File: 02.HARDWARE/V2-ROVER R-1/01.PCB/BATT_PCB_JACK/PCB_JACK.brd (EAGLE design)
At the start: 19.3 x 10.1 mm, 2 parts

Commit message: Connector Jack
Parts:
- removed PAD1, PAD2: WIREPADSMD2,54-5,08, wirepad:SMD2,54-5,08
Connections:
- removed net GND: PAD1.1
- removed net VCC: PAD2.1
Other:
- board size 19.3 x 10.1 mm -> 18.3 x 9.1 mm
- board text added: "+"
- board text added: "-"
- board text added: "2"

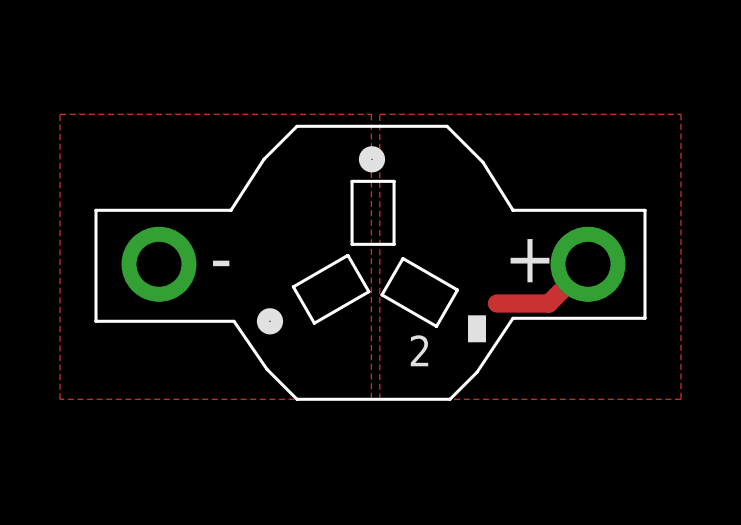
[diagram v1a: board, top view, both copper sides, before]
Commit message: Modificacion Conector Jack #37
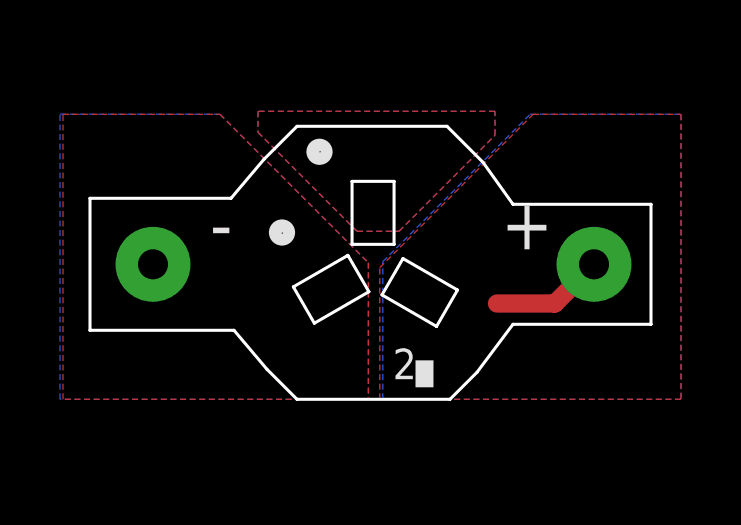
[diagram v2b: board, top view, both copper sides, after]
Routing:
- added copper zone on layer 16, net GND
- added copper zone on layer 1, net NOCONNET
- added copper zone on layer 16, net NOCONNET
- added copper zone on layer 16, net VCC
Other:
- board size 18.3 x 9.1 mm -> 18.7 x 9.1 mm

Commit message: Close #37
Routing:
- net VCC: vias 1 -> 5
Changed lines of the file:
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@@
 <grid distance="0.1" unitdist="mm" unit="mm" style="lines" multiple="1" display="yes" altdistance="5" altunitdist="mil" altunit="mil"/>
 <layers>
-<layer number="1" name="Top" color="4" fill="1" visible="yes" active="yes"/>
+<layer number="1" name="Top" color="4" fill="1" visible="no" active="yes"/>
 <layer number="2" name="Route2" color="16" fill="1" visible="no" active="no"/>
 <layer number="15" name="Route15" color="23" fill="1" visible="no" active="no"/>
-<layer number="16" name="Bottom" color="1" fill="1" visible="no" active="yes"/>
+<layer number="16" name="Bottom" color="1" fill="1" visible="yes" active="yes"/>
 <layer number="17" name="Pads" color="2" fill="1" visible="yes" active="yes"/>
 <layer number="18" name="Vias" color="2" fill="1" visible="yes" active="yes"/>
 <layer number="19" name="Unrouted" color="6" fill="1" visible="yes" active="yes"/>
-<layer number="20" name="Dimension" color="24" fill="1" visible="yes" active="yes"/>
-<layer number="21" name="tPlace" color="7" fill="1" visible="yes" active="yes"/>
-<layer number="22" name="bPlace" color="7" fill="1" visible="no" active="yes"/>
-<layer number="23" name="tOrigins" color="15" fill="1" visible="yes" active="yes"/>
-<layer number="24" name="bOrigins" color="15" fill="1" visible="no" active="yes"/>
-<layer number="25" name="tNames" color="7" fill="1" visible="yes" active="yes"/>
-<layer number="26" name="bNames" color="7" fill="1" visible="no" active="yes"/>
+<layer number="20" name="Dimension" color="24" fill="1" visible="no" active="yes"/>
+<layer number="21" name="tPlace" color="7" fill="1" visible="no" active="yes"/>
+<layer number="22" name="bPlace" color="7" fill="1" visible="yes" active="yes"/>
+<layer number="23" name="tOrigins" color="15" fill="1" visible="no" active="yes"/>
+<layer number="24" name="bOrigins" color="15" fill="1" visible="yes" active="yes"/>
+<layer number="25" name="tNames" color="7" fill="1" visible="no" active="yes"/>
+<layer number="26" name="bNames" color="7" fill="1" visible="yes" active="yes"/>
 <layer number="27" name="tValues" color="7" fill="1" visible="no" active="yes"/>
 <layer number="28" name="bValues" color="7" fill="1" visible="no" active="yes"/>
@@
 <layer number="37" name="tTest" color="7" fill="1" visible="no" active="yes"/>
 <layer number="38" name="bTest" color="7" fill="1" visible="no" active="yes"/>
-<layer number="39" name="tKeepout" color="4" fill="11" visible="yes" active="yes"/>
-<layer number="40" name="bKeepout" color="1" fill="11" visible="no" active="yes"/>
-<layer number="41" name="tRestrict" color="4" fill="10" visible="yes" active="yes"/>
-<layer number="42" name="bRestrict" color="1" fill="10" visible="no" active="yes"/>
+<layer number="39" name="tKeepout" color="4" fill="11" visible="no" active="yes"/>
+<layer number="40" name="bKeepout" color="1" fill="11" visible="yes" active="yes"/>
+<layer number="41" name="tRestrict" color="4" fill="10" visible="no" active="yes"/>
+<layer number="42" name="bRestrict" color="1" fill="10" visible="yes" active="yes"/>
 <layer number="43" name="vRestrict" color="2" fill="10" visible="no" active="yes"/>
 <layer number="44" name="Drills" color="7" fill="1" visible="no" active="yes"/>
@@
 <layer number="49" name="Reference" color="7" fill="1" visible="no" active="yes"/>
 <layer number="50" name="dxf" color="7" fill="1" visible="no" active="no"/>
-<layer number="51" name="tDocu" color="7" fill="1" visible="yes" active="yes"/>
-<layer number="52" name="bDocu" color="7" fill="1" visible="no" active="yes"/>
+<layer number="51" name="tDocu" color="7" fill="1" visible="no" active="yes"/>
+<layer number="52" name="bDocu" color="7" fill="1" visible="yes" active="yes"/>
 <layer number="53" name="tGND_GNDA" color="7" fill="9" visible="no" active="no"/>
 <layer number="54" name="bGND_GNDA" color="1" fill="9" visible="no" active="no"/>
@@
 <vertex x="81.9" y="73.1"/>
 </polygon>
+<via x="73.8" y="78.5" extent="1-16" drill="0.35"/>
+<via x="74.8" y="78.1" extent="1-16" drill="0.35"/>
+<via x="73.9" y="74.7" extent="1-16" drill="0.35"/>
+<via x="72.3" y="75.7" extent="1-16" drill="0.35"/>
 </signal>
 <signal name="GND">
@@
 <vertex x="66.53155625" y="82.6"/>
 </polygon>
+<via x="68.4" y="77.8" extent="1-16" drill="0.35"/>
+<via x="69.6" y="78.5" extent="1-16" drill="0.35"/>
+<via x="69.8" y="74.7" extent="1-16" drill="0.35"/>
+<via x="71.2" y="75.1" extent="1-16" drill="0.35"/>
 </signal>
 <signal name="NOCONNET">

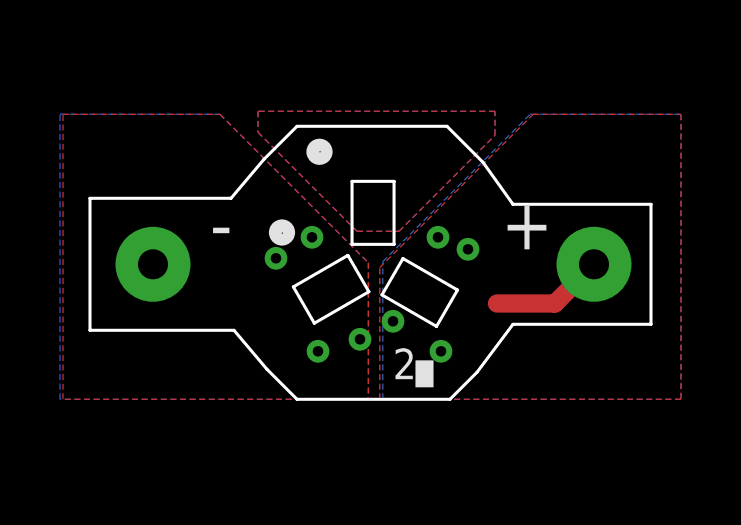
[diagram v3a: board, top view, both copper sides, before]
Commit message: Ajustes PCBs
Cambio en el pcb de cheyenne para que entre en el adapatador de la universal.
Cambio en el pcb del pogo para que se ajuste mejor a los adaptadores de la universal
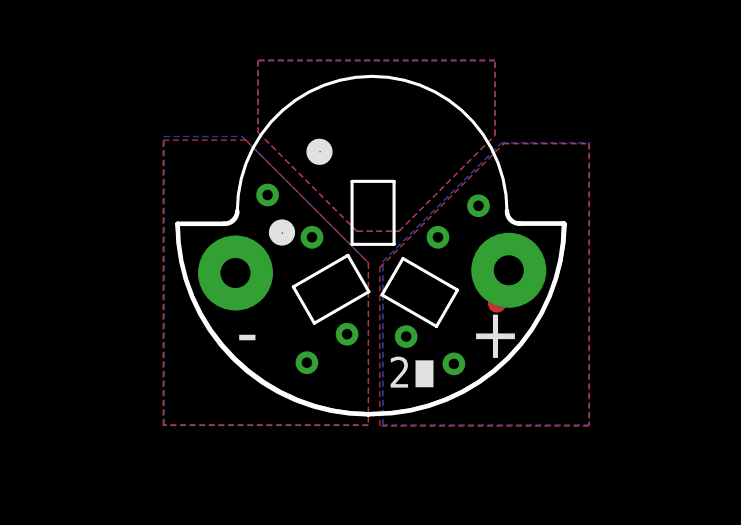
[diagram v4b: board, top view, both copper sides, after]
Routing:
- net VCC: track 3.77 -> 1.27 mm
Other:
- board size 18.7 x 9.1 mm -> 12.9 x 11.3 mm

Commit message: ajuste y separacion de los taladros de soldadura
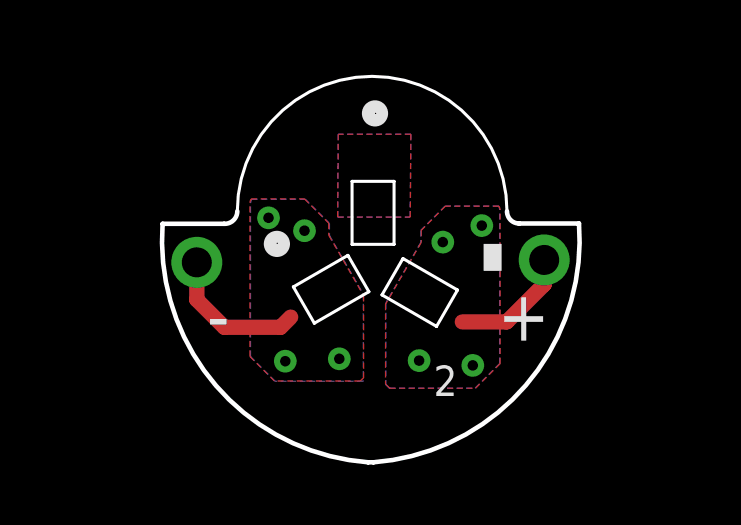
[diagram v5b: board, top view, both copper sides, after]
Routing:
- net GND: track 0.00 -> 4.90 mm
- net VCC: track 1.27 -> 4.06 mm
- added copper zone on layer 1, net S$1
- added copper zone on layer 16, net S$2
- removed copper zone on layer 1, net NOCONNET
- removed copper zone on layer 16, net NOCONNET
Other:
- board size 12.9 x 11.3 mm -> 13.9 x 12.9 mm

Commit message: Cierra issue #76 - Listo para pedido a PCBWAY
Mejoras para que no toque con mecanica
Mejora para evitar que se desuelden los cables por calentamiento del conecgtor
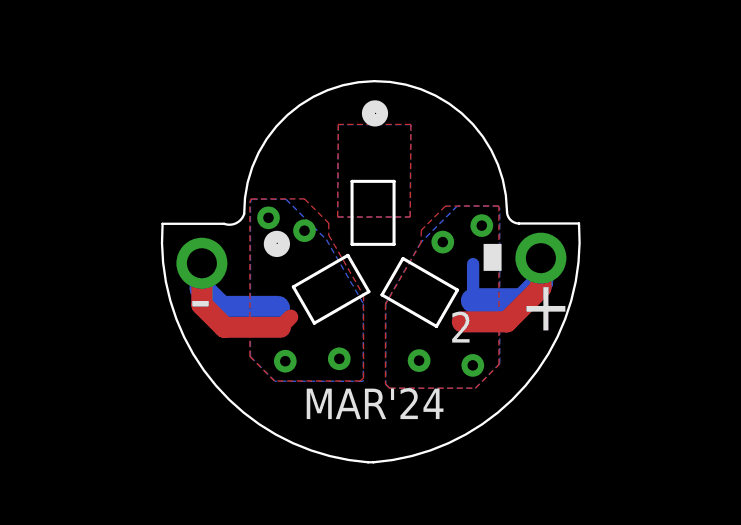
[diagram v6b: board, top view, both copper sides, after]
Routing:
- net VCC: track 4.06 -> 8.61 mm
- net GND: track 4.90 -> 8.44 mm
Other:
- board size 13.9 x 12.9 mm -> 13.9 x 12.7 mm
- board text added: "MAR'24"
